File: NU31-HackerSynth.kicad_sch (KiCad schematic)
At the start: 140 parts, among them J2 AudioJack3, J3 Barrel_Jack, J4 AudioJack2_SwitchT, J5 AudioJack2_SwitchT, J6 AudioJack2_SwitchT, J7 Eurorack Power, Q1 BC547, Q2 BC547, Q3 BC547, Q4 BC547, SW1 SW_DPDT, SW2 SW_SPDT, SW3 SW_Rotary_1x8_MP, U1 LM358, U2 LM358, U3 LM358, U4 CD4017, U5 LM358, U6 LM358, U7 LM358

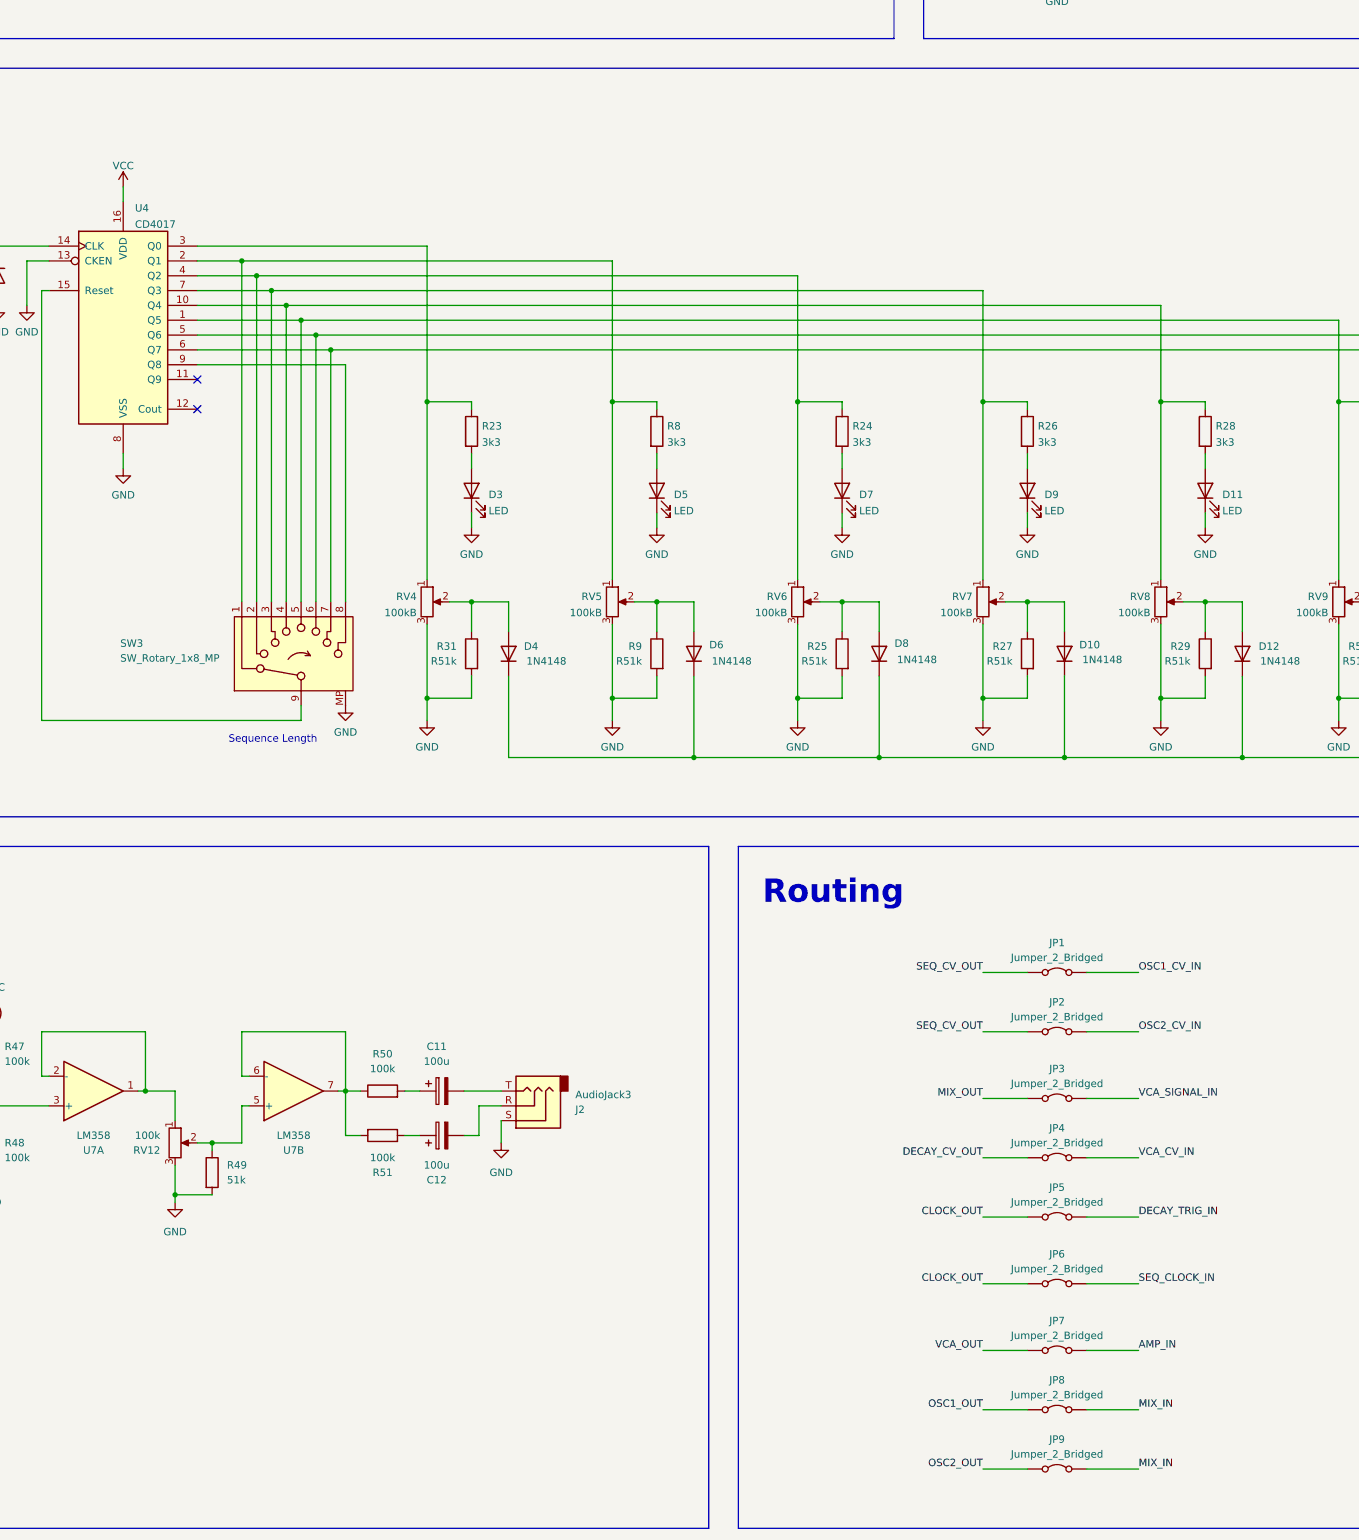
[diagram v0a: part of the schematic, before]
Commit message: added decoupling cap for CD4017, replaced all routing jumpers with one pin header
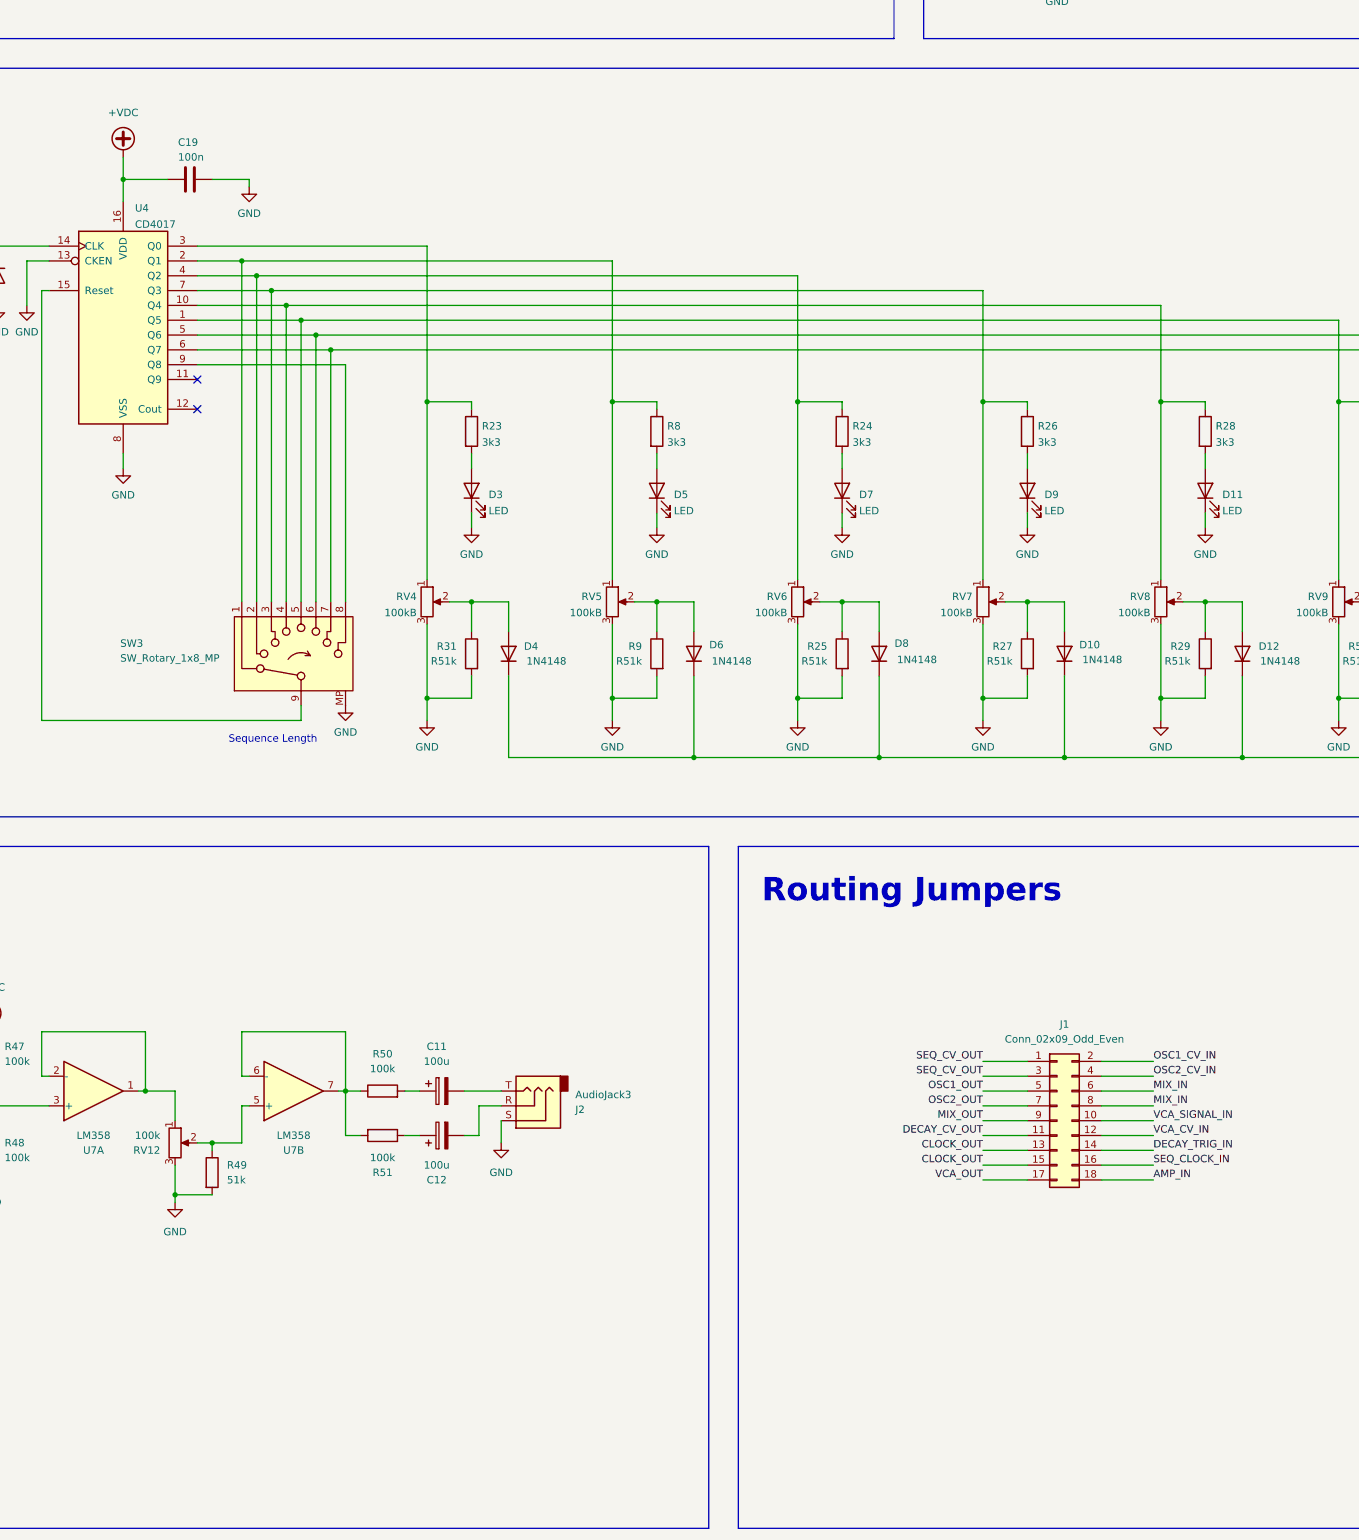
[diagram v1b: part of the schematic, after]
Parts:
- removed JP1, JP2, JP3, JP4, JP5, JP6, JP7, JP8, JP9: Jumper_2_Bridged, Connector_PinHeader_2.54mm:PinHeader_1x02_P2.54mm_Vertical, symbol Jumper:Jumper_2_Bridged
- added C19: 100n, Capacitor_THT:C_Disc_D5.1mm_W3.2mm_P5.00mm, symbol Device:C
- added J1: Conn_02x09_Odd_Even, Connector_PinHeader_2.54mm:PinHeader_2x09_P2.54mm_Vertical, symbol Connector_Generic:Conn_02x09_Odd_Even
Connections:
- net VCC is gone; now on net +VDC: U4.16 (VDD)
- net +VDC: now also C19.2
- net AMP_IN: now also J1.18 (Pin_18)
- net CLOCK_OUT: now also J1.13 (Pin_13), J1.15 (Pin_15)
- net DECAY_CV_OUT: now also J1.11 (Pin_11)
- net DECAY_TRIG_IN: now also J1.14 (Pin_14)
- net GND: now also C19.1
- net MIX_IN: now also J1.6 (Pin_6), J1.8 (Pin_8)
- net MIX_OUT: now also J1.9 (Pin_9)
- net OSC1_CV_IN: now also J1.2 (Pin_2)
- net OSC1_OUT: now also J1.5 (Pin_5)
- net OSC2_CV_IN: now also J1.4 (Pin_4)
- net OSC2_OUT: now also J1.7 (Pin_7)
- net SEQ_CLOCK_IN: now also J1.16 (Pin_16)
- net SEQ_CV_OUT: now also J1.1 (Pin_1), J1.3 (Pin_3)
- net VCA_CV_IN: now also J1.12 (Pin_12)
- net VCA_OUT: now also J1.17 (Pin_17)
- net VCA_SIGNAL_IN: now also J1.10 (Pin_10)
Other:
- note added: "Routing Jumpers"
- note removed: "Routing"

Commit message: Changed slider-switches to push-button and toggle switch, renamed mixer pins to tone
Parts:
- renumbered RV13 to RV10, RV14 to RV11, RV10 to RV13, RV11 to RV14
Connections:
- net MIX_IN renamed TONE_IN
- net MIX_OUT renamed TONE_OUT
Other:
- note removed: "Mixer/tone"
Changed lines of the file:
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@@
 		)
 	)
-	(text "Mixer/tone"
+	(text "Tone"
 		(exclude_from_sim no)
 		(at 143.51 129.286 0)
@@
 		)
 	)
-	(label "MIX_OUT"
+	(label "TONE_OUT"
 		(at 222.25 508 180)
 		(effects
@@
 		)
 	)
-	(label "MIX_IN"
+	(label "TONE_IN"
 		(at 163.83 166.37 180)
 		(effects
@@
 		)
 	)
-	(label "MIX_IN"
+	(label "TONE_IN"
 		(at 251.46 502.92 0)
 		(effects
@@
 		)
 	)
-	(label "MIX_OUT"
+	(label "TONE_OUT"
 		(at 220.98 172.72 0)
 		(effects
@@
 		)
 	)
-	(label "MIX_IN"
+	(label "TONE_IN"
 		(at 251.46 505.46 0)
 		(effects
@@
 		(dnp no)
 		(fields_autoplaced yes)
-		(property "Reference" "RV13"
+		(property "Reference" "RV10"
 			(at 314.4521 418.1915 0)
 			(effects
@@
 			(project "NU31-HackerSynth"
 				(path "/151a4108-ccd8-4864-9fa1-a2e140a3decb"
-					(reference "RV13")
+					(reference "RV10")
 					(unit 1)
 				)
@@
 		(dnp no)
 		(fields_autoplaced yes)
-		(property "Reference" "RV11"
+		(property "Reference" "RV14"
 			(at 303.53 276.86 90)
 			(effects
@@
 			(project "NU31-HackerSynth"
 				(path "/151a4108-ccd8-4864-9fa1-a2e140a3decb"
-					(reference "RV11")
+					(reference "RV14")
 					(unit 1)
 				)
@@
 		(dnp no)
 		(fields_autoplaced yes)
-		(property "Reference" "RV14"
+		(property "Reference" "RV11"
 			(at 346.2021 418.1915 0)
 			(effects
@@
 			(project "NU31-HackerSynth"
 				(path "/151a4108-ccd8-4864-9fa1-a2e140a3decb"
-					(reference "RV14")
+					(reference "RV11")
 					(unit 1)
 				)
@@
 		(on_board yes)
 		(dnp no)
-		(property "Reference" "RV10"
+		(property "Reference" "RV13"
 			(at 133.35 280.6701 0)
 			(effects
@@
 			(project "NU31-HackerSynth"
 				(path "/151a4108-ccd8-4864-9fa1-a2e140a3decb"
-					(reference "RV10")
+					(reference "RV13")
 					(unit 1)
 				)

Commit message: Board layout is ready. Also fixed some wrong polarity issues in the schematics
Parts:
- C8: footprint Diode_THT:D_A-405_P10.16mm_Horizontal -> Capacitor_THT:CP_Radial_D5.0mm_P2.50mm
- J2: value AudioJack3 -> GREEN
- SW1: footprint Button_Switch_THT:SW_CK_JS202011CQN_DPDT_Straight -> SpaceCow:ToggleSwitch_MTS-202_DPDT
- SW2: footprint Button_Switch_THT:SW_Slide_SPDT_Straight_CK_OS102011MS2Q -> SpaceCow:8x8_DPDT_Push_Button; symbol Switch:SW_SPDT -> Switch:SW_Slide_DPDT
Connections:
- net +VDC: now also U6.8 (V+), U7.8 (V+); no longer U6.4 (V-), U7.4 (V-)
- net GND: now also SW2.4 (A), SW2.5 (B), SW2.6 (C), U6.4 (V-), U7.4 (V-); no longer U6.8 (V+), U7.8 (V+)

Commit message: Updated OSC shape switch footprint, optimized routing for decoupling capacitors and ground plane
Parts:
- SW1: footprint SpaceCow:ToggleSwitch_MTS-202_DPDT -> SpaceCow:DPDT-subminiature-toggle
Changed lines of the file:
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@@
 			)
 		)
-		(property "Footprint" "SpaceCow:ToggleSwitch_MTS-202_DPDT"
+		(property "Footprint" "SpaceCow:DPDT-subminiature-toggle"
 			(at 53.34 154.94 0)
 			(effects

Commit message: fixed clock switch pinout and footprint
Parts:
- removed SW2: SW_SPDT, SpaceCow:8x8_DPDT_Push_Button, symbol Switch:SW_Slide_DPDT
- added SW4: SW_DPST, SpaceCow:8x8_DPDT_Push_Button, symbol Switch:SW_DPST
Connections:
- net GND: now also SW4.1, SW4.2
- net SEQ_CLOCK_IN: now also SW4.3
- net at R59.2: now also SW4.4
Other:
- moved on the sheet: C19, D10, D11, D12, D13, D14, D15, D16, D17, D18, D20, D3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

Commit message: Fine-tuned the value, fixed power polarity in the schematics
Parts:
- C1, C6: value 50n -> 10n
- R25, R27, R29, R31, R52, R54, R56, R9: value R51k -> 51k
- R50, R51: value 100k -> 1k
- R58: value 3k -> 3k3
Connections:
- net GND: now also J3.2; no longer J3.1
- net at D2.2 (A), J7.10 (Pin_10), J7.9 (Pin_9): now also J3.1; no longer J3.2
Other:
- note added: "Clock Output"
- note removed: "External Clock Output"
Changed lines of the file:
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@@
 		)
 	)
-	(text "External Clock Output"
+	(text "Clock Output"
 		(exclude_from_sim no)
 		(at 376.428 263.144 0)
@@
 			)
 		)
-		(property "Value" "R51k"
+		(property "Value" "51k"
 			(at 323.85 429.2599 0)
 			(effects
@@
 			)
 		)
-		(property "Value" "R51k"
+		(property "Value" "51k"
 			(at 290.83 429.2599 0)
 			(effects
@@
 			)
 		)
-		(property "Value" "100k"
+		(property "Value" "1k"
 			(at 119.38 514.35 90)
 			(effects
@@
 			)
 		)
-		(property "Value" "3k"
+		(property "Value" "3k3"
 			(at 198.12 176.53 0)
 			(effects
@@
 			)
 		)
-		(property "Value" "R51k"
+		(property "Value" "51k"
 			(at 198.12 429.2599 0)
 			(effects
@@
 			)
 		)
-		(property "Value" "R51k"
+		(property "Value" "51k"
 			(at 166.37 429.2599 0)
 			(effects
@@
 			)
 		)
-		(property "Value" "50n"
+		(property "Value" "10n"
 			(at 318.77 40.64 90)
 			(effects
@@
 		(lib_id "Connector:Barrel_Jack")
 		(at 332.74 491.49 0)
-		(mirror x)
 		(unit 1)
 		(exclude_from_sim no)
@@
 		(dnp no)
 		(property "Reference" "J3"
-			(at 332.74 500.38 0)
+			(at 332.74 482.6 0)
 			(effects
 				(font
@@
 		)
 		(property "Value" "Barrel_Jack"
-			(at 332.74 497.84 0)
+			(at 332.74 485.14 0)
 			(effects
 				(font
@@
 		)
 		(property "Footprint" "Connector_BarrelJack:BarrelJack_Wuerth_6941xx301002"
-			(at 334.01 490.474 0)
+			(at 334.01 492.506 0)
 			(effects
 				(font
@@
 		)
 		(property "Datasheet" "~"
-			(at 334.01 490.474 0)
+			(at 334.01 492.506 0)
 			(effects
 				(font
@@
 			)
 		)
-		(property "Value" "50n"
+		(property "Value" "10n"
 			(at 109.22 39.37 90)
 			(effects
@@
 			)
 		)
-		(property "Value" "R51k"
+		(property "Value" "51k"
 			(at 355.6 429.2599 0)
 			(effects
@@
 			)
 		)
-		(property "Value" "100k"
+		(property "Value" "1k"
 			(at 119.38 499.11 90)
 			(effects
@@
 			)
 		)
-		(property "Value" "R51k"
+		(property "Value" "51k"
 			(at 260.35 429.2599 0)
 			(effects
@@
 			)
 		)
-		(property "Value" "R51k"
+		(property "Value" "51k"
 			(at 134.62 429.2599 0)
 			(effects
@@
 			)
 		)
-		(property "Value" "R51k"
+		(property "Value" "51k"
 			(at 229.87 429.2599 0)
 			(effects
